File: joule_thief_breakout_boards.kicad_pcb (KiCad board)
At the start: 2 copper layers, 20.4 x 53.3 mm, 15 parts, among them J1 Conn_01x02, J2 Conn_01x02, J3 Conn_01x02, J4 Conn_01x02, J5 Conn_01x02, J6 Conn_01x03, J7 Conn_01x03, J8 Conn_01x03, Q1 BC817-40, U1 INA180

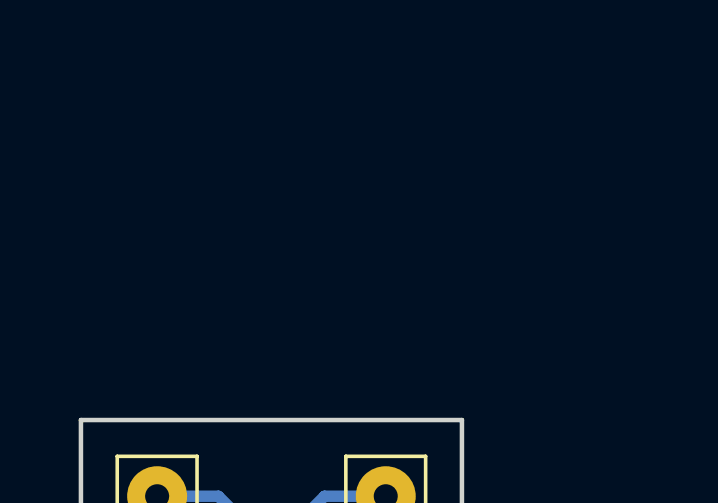
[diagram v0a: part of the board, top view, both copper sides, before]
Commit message: add SRF3216 breakout PCB layout
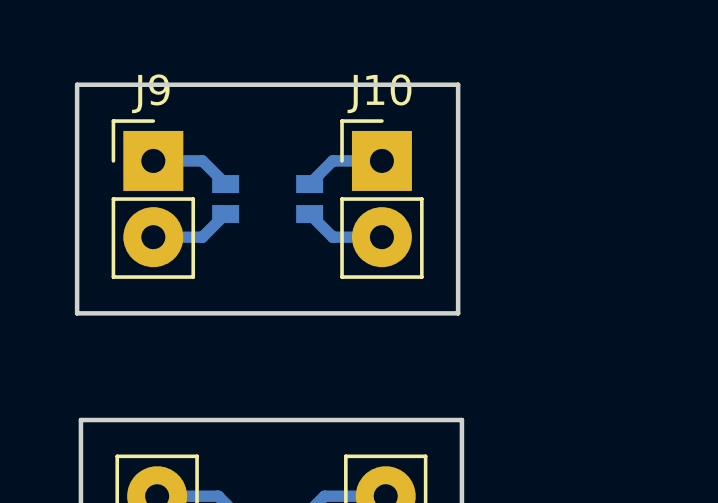
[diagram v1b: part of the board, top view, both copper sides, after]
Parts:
- added FL3: SRF3216-222Y, lib_fp:SRF3216_Bourns_CMI, B.Cu at (146.1, 87.9)
- added J10: Conn_01x02, lib_fp:Etch_Pin_Header_Straight_1x02_Pitch2.54mm, F.Cu at (149.9, 86.6)
- added J9: Conn_01x02, lib_fp:Etch_Pin_Header_Straight_1x02_Pitch2.54mm, F.Cu at (142.2, 86.6)
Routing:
- net Net-(FL3-Pad3): track 0.00 -> 2.73 mm
- net Net-(FL3-Pad2): track 0.00 -> 2.73 mm
- net Net-(FL3-Pad4): track 0.00 -> 2.73 mm
- net Net-(FL3-Pad1): track 0.00 -> 2.73 mm
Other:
- board size 20.4 x 53.3 mm -> 20.4 x 64.5 mm
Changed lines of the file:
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@@
 (kicad_pcb (version 4) (host pcbnew 4.0.7)
   (general
-    (links 25)
+    (links 29)
     (no_connects 0)
-    (area 137.492381 94.485 162.35462 149.455)
+    (area 139.624999 95.174999 160.222001 148.665001)
     (thickness 1.6)
-    (drawings 20)
-    (tracks 47)
+    (drawings 24)
+    (tracks 55)
     (zones 0)
-    (modules 15)
-    (nets 19)
+    (modules 18)
+    (nets 23)
   )
   (page A4)
@@
   )
   (setup
-    (last_trace_width 0.25)
+    (last_trace_width 0.381)
     (user_trace_width 0.381)
     (trace_clearance 0.2)
@@
   (net 17 "Net-(J8-Pad2)")
   (net 18 "Net-(J8-Pad3)")
+  (net 19 "Net-(FL3-Pad1)")
+  (net 20 "Net-(FL3-Pad2)")
+  (net 21 "Net-(FL3-Pad3)")
+  (net 22 "Net-(FL3-Pad4)")
   (net_class Default "This is the default net class."
     (clearance 0.2)
@@
     (add_net "Net-(FL2-Pad3)")
     (add_net "Net-(FL2-Pad4)")
+    (add_net "Net-(FL3-Pad1)")
+    (add_net "Net-(FL3-Pad2)")
+    (add_net "Net-(FL3-Pad3)")
+    (add_net "Net-(FL3-Pad4)")
     (add_net "Net-(J6-Pad1)")
     (add_net "Net-(J6-Pad2)")
@@
     )
   )
+  (module lib_fp:SRF3216_Bourns_CMI (layer B.Cu)
+    (at 146.05 87.884)
+    (fp_text reference FL3 (at 0 -1.7) (layer B.SilkS)
+      (effects (font (size 1 1) (thickness 0.15)) (justify mirror))
+    )
+    (fp_text value SRF3216-222Y (at 0 0) (layer B.Fab)
+      (effects (font (size 1 1) (thickness 0.15)) (justify mirror))
+    )
+    (fp_circle (center -1.95 -0.9) (end -1.95 -0.85) (layer B.SilkS) (width 0.15))
+    (fp_line (start -1.6 0.8) (end 1.6 0.8) (layer B.SilkS) (width 0.15))
+    (fp_line (start 1.6 0.8) (end 1.6 -0.8) (layer B.SilkS) (width 0.15))
+    (fp_line (start 1.6 -0.8) (end -1.6 -0.8) (layer B.SilkS) (width 0.15))
+    (fp_line (start -1.6 -0.8) (end -1.6 0.8) (layer B.SilkS) (width 0.15))
+    (pad 1 smd rect (at -1.4 -0.5) (size 0.9 0.6) (layers B.Cu B.Paste B.Mask)
+      (net 19 "Net-(FL3-Pad1)"))
+    (pad 2 smd rect (at 1.4 -0.5) (size 0.9 0.6) (layers B.Cu B.Paste B.Mask)
+      (net 20 "Net-(FL3-Pad2)"))
+    (pad 3 smd rect (at 1.4 0.5) (size 0.9 0.6) (layers B.Cu B.Paste B.Mask)
+      (net 21 "Net-(FL3-Pad3)"))
+    (pad 4 smd rect (at -1.4 0.5) (size 0.9 0.6) (layers B.Cu B.Paste B.Mask)
+      (net 22 "Net-(FL3-Pad4)"))
+  )
+  (module lib_fp:Etch_Pin_Header_Straight_1x02_Pitch2.54mm (layer F.Cu)
+    (at 142.24 86.614)
+    (descr "Through hole straight pin header, 1x02, 2.54mm pitch, single row")
+    (tags "Through hole pin header THT 1x02 2.54mm single row")
+    (fp_text reference J9 (at 0 -2.33) (layer F.SilkS)
+      (effects (font (size 1 1) (thickness 0.15)))
+    )
+    (fp_text value Conn_01x02 (at 0 4.87) (layer F.Fab)
+      (effects (font (size 1 1) (thickness 0.15)))
+    )
+    (fp_line (start -0.635 -1.27) (end 1.27 -1.27) (layer F.Fab) (width 0.1))
+    (fp_line (start 1.27 -1.27) (end 1.27 3.81) (layer F.Fab) (width 0.1))
+    (fp_line (start 1.27 3.81) (end -1.27 3.81) (layer F.Fab) (width 0.1))
+    (fp_line (start -1.27 3.81) (end -1.27 -0.635) (layer F.Fab) (width 0.1))
+    (fp_line (start -1.27 -0.635) (end -0.635 -1.27) (layer F.Fab) (width 0.1))
+    (fp_line (start -1.33 3.87) (end 1.33 3.87) (layer F.SilkS) (width 0.12))
+    (fp_line (start -1.33 1.27) (end -1.33 3.87) (layer F.SilkS) (width 0.12))
+    (fp_line (start 1.33 1.27) (end 1.33 3.87) (layer F.SilkS) (width 0.12))
+    (fp_line (start -1.33 1.27) (end 1.33 1.27) (layer F.SilkS) (width 0.12))
+    (fp_line (start -1.33 0) (end -1.33 -1.33) (layer F.SilkS) (width 0.12))
+    (fp_line (start -1.33 -1.33) (end 0 -1.33) (layer F.SilkS) (width 0.12))
+    (fp_line (start -1.8 -1.8) (end -1.8 4.35) (layer F.CrtYd) (width 0.05))
+    (fp_line (start -1.8 4.35) (end 1.8 4.35) (layer F.CrtYd) (width 0.05))
+    (fp_line (start 1.8 4.35) (end 1.8 -1.8) (layer F.CrtYd) (width 0.05))
+    (fp_line (start 1.8 -1.8) (end -1.8 -1.8) (layer F.CrtYd) (width 0.05))
+    (fp_text user %R (at 0 1.27 90) (layer F.Fab)
+      (effects (font (size 1 1) (thickness 0.15)))
+    )
+    (pad 1 thru_hole rect (at 0 0) (size 2 2) (drill 0.8) (layers *.Cu *.Mask)
+      (net 19 "Net-(FL3-Pad1)"))
+    (pad 2 thru_hole oval (at 0 2.54) (size 2 2) (drill 0.8) (layers *.Cu *.Mask)
+      (net 22 "Net-(FL3-Pad4)"))
+    (model ${KISYS3DMOD}/Pin_Headers.3dshapes/Pin_Header_Straight_1x02_Pitch2.54mm.wrl
+      (at (xyz 0 0 0))
+      (scale (xyz 1 1 1))
+      (rotate (xyz 0 0 0))
+    )
+  )
+  (module lib_fp:Etch_Pin_Header_Straight_1x02_Pitch2.54mm (layer F.Cu)
+    (at 149.86 86.614)
+    (descr "Through hole straight pin header, 1x02, 2.54mm pitch, single row")
+    (tags "Through hole pin header THT 1x02 2.54mm single row")
+    (fp_text reference J10 (at 0 -2.33) (layer F.SilkS)
+      (effects (font (size 1 1) (thickness 0.15)))
+    )
+    (fp_text value Conn_01x02 (at 0 4.87) (layer F.Fab)
+      (effects (font (size 1 1) (thickness 0.15)))
+    )
+    (fp_line (start -0.635 -1.27) (end 1.27 -1.27) (layer F.Fab) (width 0.1))
+    (fp_line (start 1.27 -1.27) (end 1.27 3.81) (layer F.Fab) (width 0.1))
+    (fp_line (start 1.27 3.81) (end -1.27 3.81) (layer F.Fab) (width 0.1))
+    (fp_line (start -1.27 3.81) (end -1.27 -0.635) (layer F.Fab) (width 0.1))
+    (fp_line (start -1.27 -0.635) (end -0.635 -1.27) (layer F.Fab) (width 0.1))
+    (fp_line (start -1.33 3.87) (end 1.33 3.87) (layer F.SilkS) (width 0.12))
+    (fp_line (start -1.33 1.27) (end -1.33 3.87) (layer F.SilkS) (width 0.12))
+    (fp_line (start 1.33 1.27) (end 1.33 3.87) (layer F.SilkS) (width 0.12))
+    (fp_line (start -1.33 1.27) (end 1.33 1.27) (layer F.SilkS) (width 0.12))
+    (fp_line (start -1.33 0) (end -1.33 -1.33) (layer F.SilkS) (width 0.12))
+    (fp_line (start -1.33 -1.33) (end 0 -1.33) (layer F.SilkS) (width 0.12))
+    (fp_line (start -1.8 -1.8) (end -1.8 4.35) (layer F.CrtYd) (width 0.05))
+    (fp_line (start -1.8 4.35) (end 1.8 4.35) (layer F.CrtYd) (width 0.05))
+    (fp_line (start 1.8 4.35) (end 1.8 -1.8) (layer F.CrtYd) (width 0.05))
+    (fp_line (start 1.8 -1.8) (end -1.8 -1.8) (layer F.CrtYd) (width 0.05))
+    (fp_text user %R (at 0 1.27 90) (layer F.Fab)
+      (effects (font (size 1 1) (thickness 0.15)))
+    )
+    (pad 1 thru_hole rect (at 0 0) (size 2 2) (drill 0.8) (layers *.Cu *.Mask)
+      (net 20 "Net-(FL3-Pad2)"))
+    (pad 2 thru_hole oval (at 0 2.54) (size 2 2) (drill 0.8) (layers *.Cu *.Mask)
+      (net 21 "Net-(FL3-Pad3)"))
+    (model ${KISYS3DMOD}/Pin_Headers.3dshapes/Pin_Header_Straight_1x02_Pitch2.54mm.wrl
+      (at (xyz 0 0 0))
+      (scale (xyz 1 1 1))
+      (rotate (xyz 0 0 0))
+    )
+  )
+  (gr_line (start 139.7 91.694) (end 139.7 84.074) (angle 90) (layer Edge.Cuts) (width 0.15))
+  (gr_line (start 152.4 91.694) (end 139.7 91.694) (angle 90) (layer Edge.Cuts) (width 0.15))
+  (gr_line (start 152.4 84.074) (end 152.4 91.694) (angle 90) (layer Edge.Cuts) (width 0.15))
+  (gr_line (start 139.7 84.074) (end 152.4 84.074) (angle 90) (layer Edge.Cuts) (width 0.15))
   (gr_line (start 149.86 148.59) (end 139.7 148.59) (angle 90) (layer Edge.Cuts) (width 0.15))
   (gr_line (start 149.86 138.43) (end 149.86 148.59) (angle 90) (layer Edge.Cuts) (width 0.15))
@@
   (segment (start 142.24 140.97) (end 144.73 140.97) (width 0.381) (layer B.Cu) (net 18))
   (segment (start 144.73 140.97) (end 146.32 142.56) (width 0.381) (layer B.Cu) (net 18))
+  (segment (start 142.24 86.614) (end 143.88 86.614) (width 0.381) (layer B.Cu) (net 19))
+  (segment (start 143.88 86.614) (end 144.65 87.384) (width 0.381) (layer B.Cu) (net 19))
+  (segment (start 149.86 86.614) (end 148.22 86.614) (width 0.381) (layer B.Cu) (net 20))
+  (segment (start 148.22 86.614) (end 147.45 87.384) (width 0.381) (layer B.Cu) (net 20))
+  (segment (start 149.86 89.154) (end 148.22 89.154) (width 0.381) (layer B.Cu) (net 21))
+  (segment (start 148.22 89.154) (end 147.45 88.384) (width 0.381) (layer B.Cu) (net 21))
+  (segment (start 142.24 89.154) (end 143.88 89.154) (width 0.381) (layer B.Cu) (net 22))
+  (segment (start 143.88 89.154) (end 144.65 88.384) (width 0.381) (layer B.Cu) (net 22))
 )

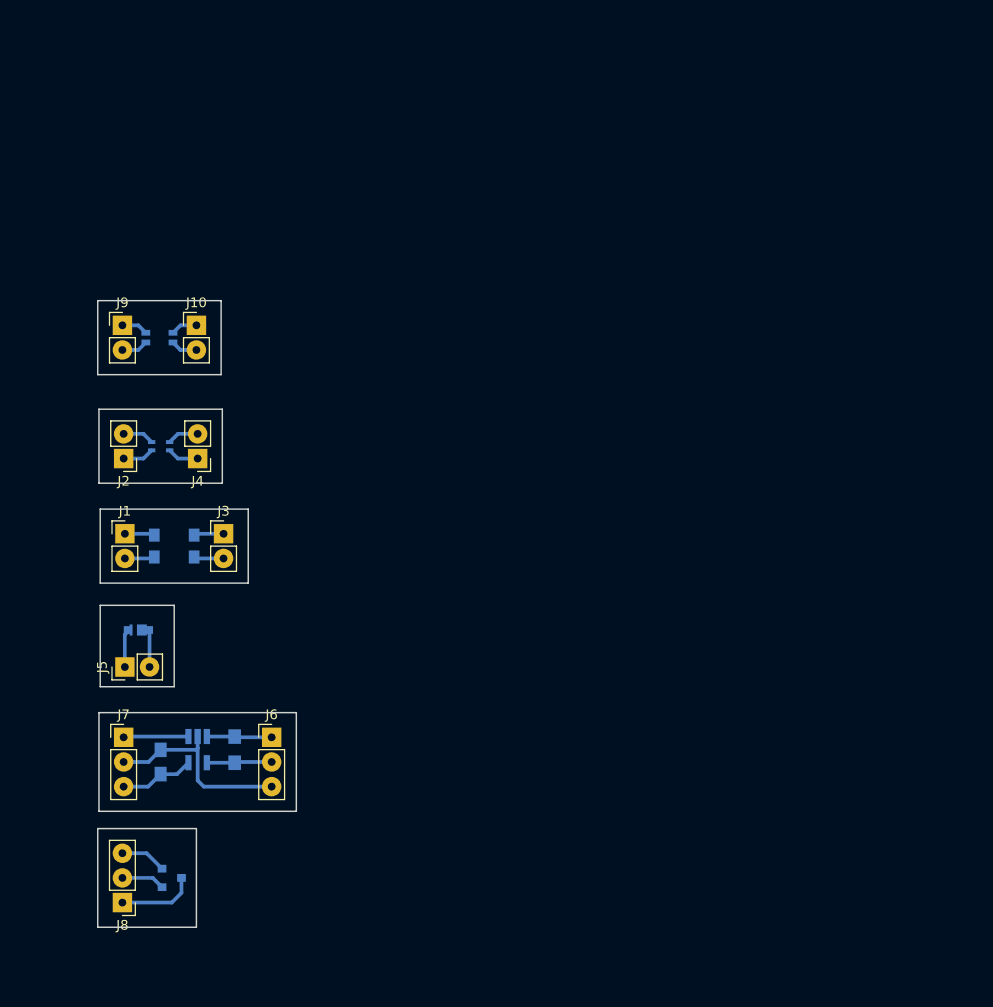
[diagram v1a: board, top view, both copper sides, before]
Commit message: add joule thief with measurement points
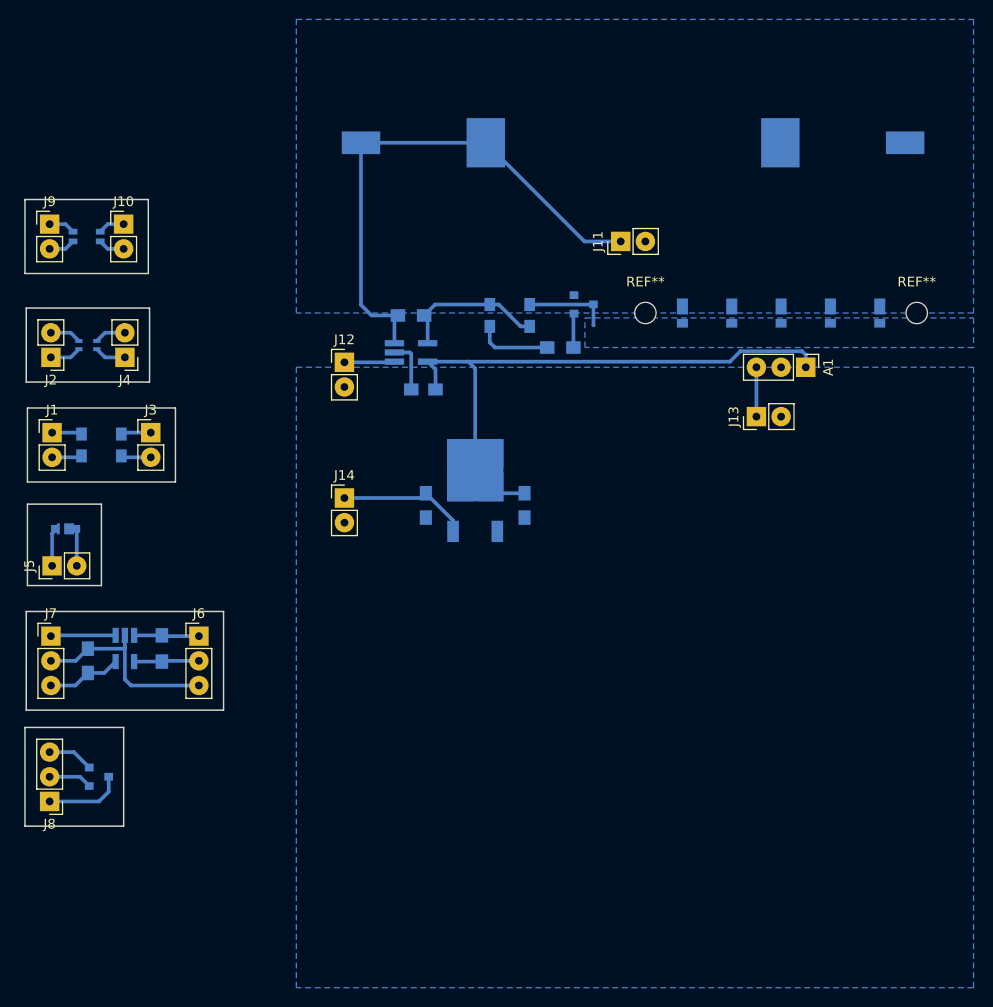
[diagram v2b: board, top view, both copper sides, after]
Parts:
- added A1: TEMT600, lib_fp:Etch_Pin_Header_Straight_1x03_Pitch2.54mm, F.Cu at (212.6, 90.9)
- added BT1: AA Cell, lib_fp:BK-53_MPD_AAClip, B.Cu at (194.8, 67.8)
- added C2: 10uF, Capacitors_SMD:C_0805_HandSoldering, B.Cu at (173.5, 105.2)
- added C3: 10uF, Capacitors_SMD:C_0805_HandSoldering, B.Cu at (183.6, 105.2)
- added C4: 0.1uF, Capacitors_SMD:C_0805_HandSoldering, B.Cu at (173.2, 93.2)
- added D2: LED, lib_fp:LED_Luminus_MP-2016, B.Cu at (199.9, 85.7)
- added D3: LED, lib_fp:LED_Luminus_MP-2016, B.Cu at (205.0, 85.7)
- added D4: LED, lib_fp:LED_Luminus_MP-2016, B.Cu at (210.1, 85.7)
- added D5: LED, lib_fp:LED_Luminus_MP-2016, B.Cu at (215.1, 85.7)
- added D6: LED, lib_fp:LED_Luminus_MP-2016, B.Cu at (220.2, 85.7)
- added FL4: Bourns_Common_Mode_Inductor, lib_fp:SRF4532_Bourns_CMI, B.Cu at (182.1, 85.6)
- added J11: Voltage, lib_fp:Etch_Pin_Header_Straight_1x02_Pitch2.54mm, F.Cu at (193.5, 78.0)
- added J12: Current, lib_fp:Etch_Pin_Header_Straight_1x02_Pitch2.54mm, F.Cu at (165.1, 90.4)
- added J13: Light, lib_fp:Etch_Pin_Header_Straight_1x02_Pitch2.54mm, F.Cu at (207.5, 96.0)
- added J14: PWR, lib_fp:Etch_Pin_Header_Straight_1x02_Pitch2.54mm, F.Cu at (165.1, 104.4)
- added Q2: BC817-40, TO_SOT_Packages_SMD:SOT-23, B.Cu at (189.7, 84.5)
- added R2: 0.1, Resistors_SMD:R_0805_HandSoldering, B.Cu at (172.0, 85.6)
- added R3: R, Resistors_SMD:R_0805_HandSoldering, B.Cu at (187.3, 88.9)
- added REF**: MountingHole_2.2mm_M2, Mounting_Holes:MountingHole_2.2mm_M2, F.Cu at (224.0, 85.3)
- added REF**: MountingHole_2.2mm_M2, Mounting_Holes:MountingHole_2.2mm_M2, F.Cu at (196.1, 85.3)
- added U2: NCP1117-3.3, TO_SOT_Packages_SMD:TO-252-2, B.Cu at (178.6, 103.6)
- added U3: INA180A4, TO_SOT_Packages_SMD:TSOT-23-5_HandSoldering, B.Cu at (172.0, 89.4)
- moved FL3 12.8 mm to (138.6, 77.5)
- moved J10 12.8 mm to (142.4, 76.2)
- moved J6 12.8 mm to (150.1, 118.6)
- moved J7 12.8 mm to (134.9, 118.6)
- moved J8 12.8 mm to (134.7, 135.6)
- moved FL1 12.8 mm to (140.1, 98.9)
- moved C1 12.8 mm to (138.7, 121.2)
- moved D1 12.8 mm to (136.0, 107.6)
- moved FL2 12.8 mm to (138.7, 88.6)
- moved J1 12.8 mm to (135.0, 97.7)
- moved J2 12.8 mm to (134.9, 89.9)
- moved J3 12.8 mm to (145.2, 97.7)
- moved J4 12.8 mm to (142.5, 89.9)
- moved J5 12.8 mm to (135.0, 111.4)
- moved J9 12.8 mm to (134.7, 76.2)
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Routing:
- net +3V3: track 0.00 -> 61.6 mm
- net Net-(BT1-Pad1): track 0.00 -> 54.9 mm
- net Net-(FL4-Pad1): track 0.00 -> 15.3 mm
- net +5V: track 0.00 -> 13.7 mm
- net Net-(D2-Pad2): track 0.00 -> 8.74 mm
- net Net-(FL4-Pad4): track 0.00 -> 7.78 mm
- net GNDA: track 0.00 -> 5.45 mm
- net Net-(J12-Pad1): track 0.00 -> 5.18 mm
- net Net-(A1-Pad3): track 0.00 -> 5.08 mm
- net Net-(Q2-Pad1): track 0.00 -> 3.52 mm
- added copper zone on B.Cu, net GND
- added copper zone on B.Cu, net GNDA
- added copper zone on B.Cu, net Net-(D2-Pad2)
